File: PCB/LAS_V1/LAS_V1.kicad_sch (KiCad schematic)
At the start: 7 parts, among them J1 Conn_01x05_Socket, J2 Screw_Terminal_01x02, J4 Screw_Terminal_01x03, J5 Red_Conn_01x02_Pin, J6 Conn_01x18_Socket, J7 Conn_01x18_Socket, J9 Screw_Terminal_01x02

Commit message: -am
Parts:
- removed J2: Screw_Terminal_01x02, symbol Connector:Screw_Terminal_01x02
- added U2: ESP32-S2-MINI-1, Espressif:ESP32-S2-MINI-1, symbol ESP lib:ESP32-S2-MINI-1
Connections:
- net GND: now also U2.1 (GND), U2.2 (GND), U2.30 (GND), U2.42 (GND), U2.43 (GND), U2.46 (GND), U2.47 (GND), U2.48 (GND), U2.49 (GND), U2.50 (GND), U2.51 (GND), U2.52 (GND), U2.53 (GND), U2.54 (GND), U2.55 (GND), U2.56 (GND), U2.57 (GND), U2.58 (GND), U2.59 (GND), U2.60 (GND), U2.61 (GND), U2.62 (GND), U2.63 (GND), U2.64 (GND), U2.65 (GND)
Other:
- added sheet USB Interface (USB_interface.kicad_sch)
- sheet Power ports: added +3.3V; removed +12V
- sheet Relay Controls ports: added none; removed D1, D2, D3, D4, D5, D6, NO2, relay2
- moved on the sheet: J5

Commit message: installing JLB, PCB mostly done
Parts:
- removed U2: ESP32-S2-MINI-1, Espressif:ESP32-S2-MINI-1, symbol ESP lib:ESP32-S2-MINI-1
- added C4 (x3): 0.1uF, symbol Device:C_Small
- added C4 (x2): 10uF, symbol Device:C_Small
- added C4: 1uF, symbol Device:C_Small
- added R1: 10k, symbol Device:R_Small_US
- added SW1, SW2: SW_Push, symbol Switch:SW_Push
- added U1: ESP32-S3-WROOM-1, Espressif:ESP32-S3-WROOM-1, symbol ESP lib:ESP32-S3-WROOM-1
- added U2: AMS1117-3.3, Package_TO_SOT_SMD:SOT-223-3_TabPin2, symbol Regulator_Linear:AMS1117-3.3
- renumbered J9 to J1, J4 to J2, J5 to J3, J1 to J4, J7 to J5
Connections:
- net GND: now also C4.2, C4.2, C4.2, C4.2, C4.2, C4.2, SW1.1, SW2.1, U1.1 (GND), U1.40 (GND), U1.41 (GND), U2.1 (GND)
- net NC1: no longer J2.1 (Pin_1)
- net NO1: no longer names the net of J2.2 (Pin_2)
- new net +3.3V: C4.1, C4.1, C4.1, R1.1, U1.2 (3V3), U2.2 (VO)
- new net BOOT_SEL: C4.1, SW1.2, U1.27 (GPIO0/BOOT)
- new net CHIP_PU: C4.1, C4.1, R1.2, SW2.2, U1.3 (EN)
- new net DIN_3.3: U1.5 (GPIO5/TOUCH5/ADC1_CH4)
- new net GPIO1: U1.38 (GPIO2/TOUCH2/ADC1_CH1)
- new net GPIO2: U1.15 (GPIO3/TOUCH3/ADC1_CH2)
- new net GPIO3: U1.4 (GPIO4/TOUCH4/ADC1_CH3)
- new net GPIO6: U1.6 (GPIO6/TOUCH6/ADC1_CH5)
- new net RX1: U1.7 (GPIO7/TOUCH7/ADC1_CH6)
- new net RXD0: U1.36 (U0RXD/GPIO44/CLK_OUT2)
- new net TXD0: U1.37 (U0TXD/GPIO43/CLK_OUT1)
- new net VCC_5V: U2.3 (VI)
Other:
- removed sheet Power
- added sheet AC Monitor (AC_Monitor_sch.kicad_sch)
- added sheet Level Shifter (Level_shifter.kicad_sch)
- sheet LEDs ports: added +5V, DIN; removed none
- sheet Relay Controls ports: added +5V, COM, relay_act; removed relay1, relay_input1, relay_input2
- sheet USB Interface ports: added +3.3V, BOOT_SEL, CHIP_PU, RXD0, TXD0, VBus, VCC_5V; removed none
- moved on the sheet: J4, J5, J6

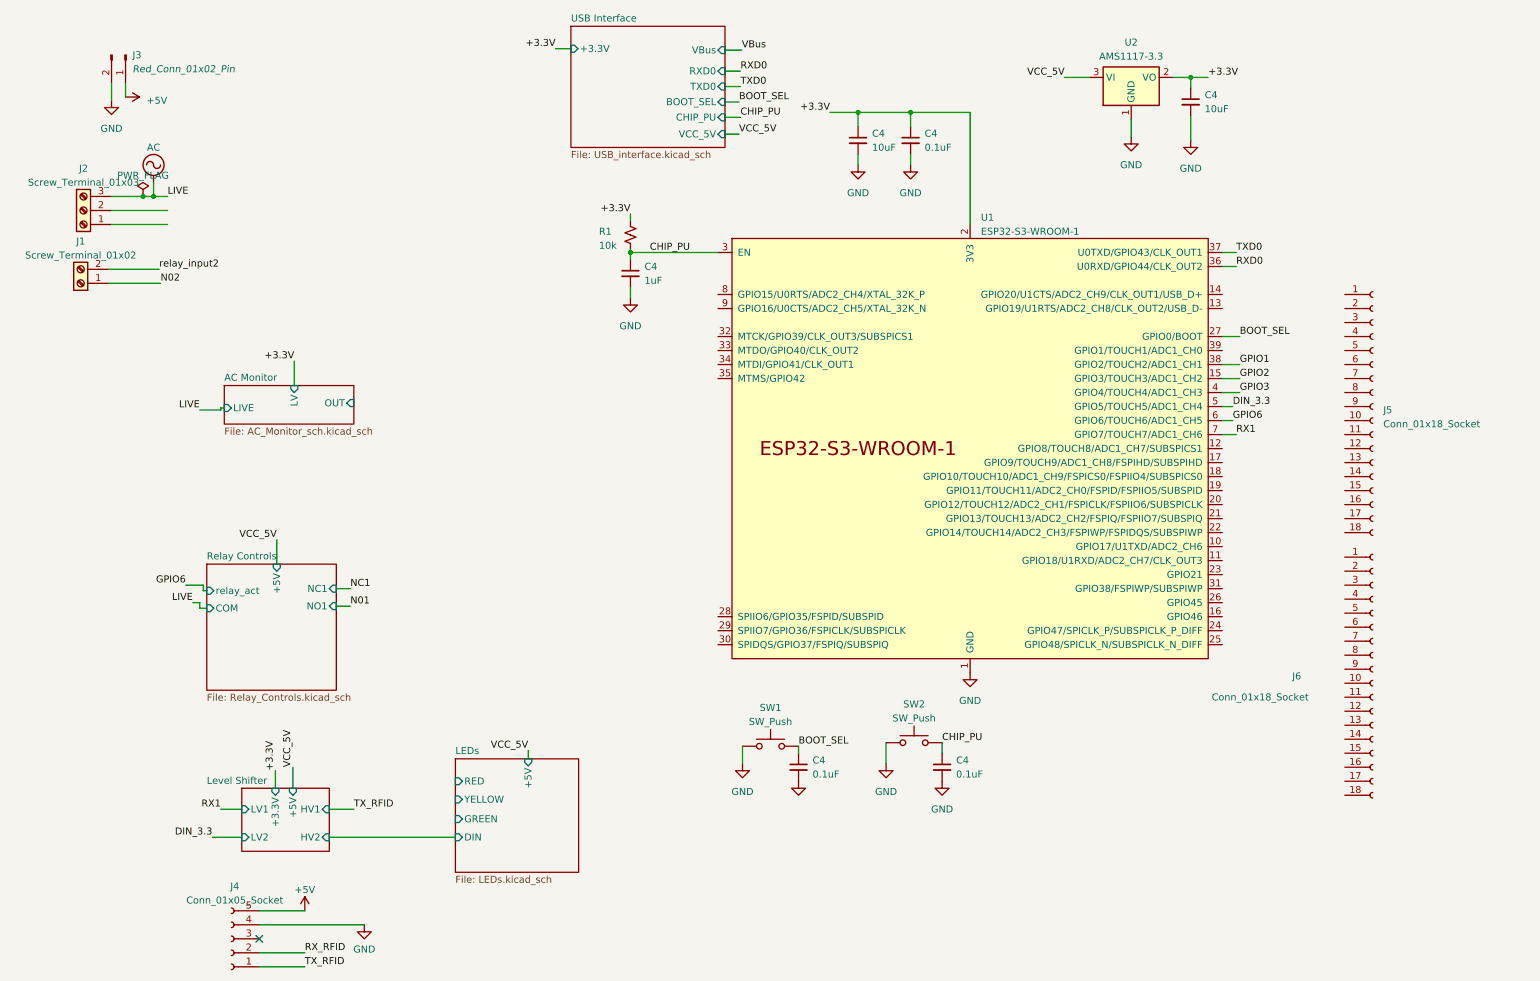
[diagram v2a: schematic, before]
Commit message: added JLBPCB part Numbers
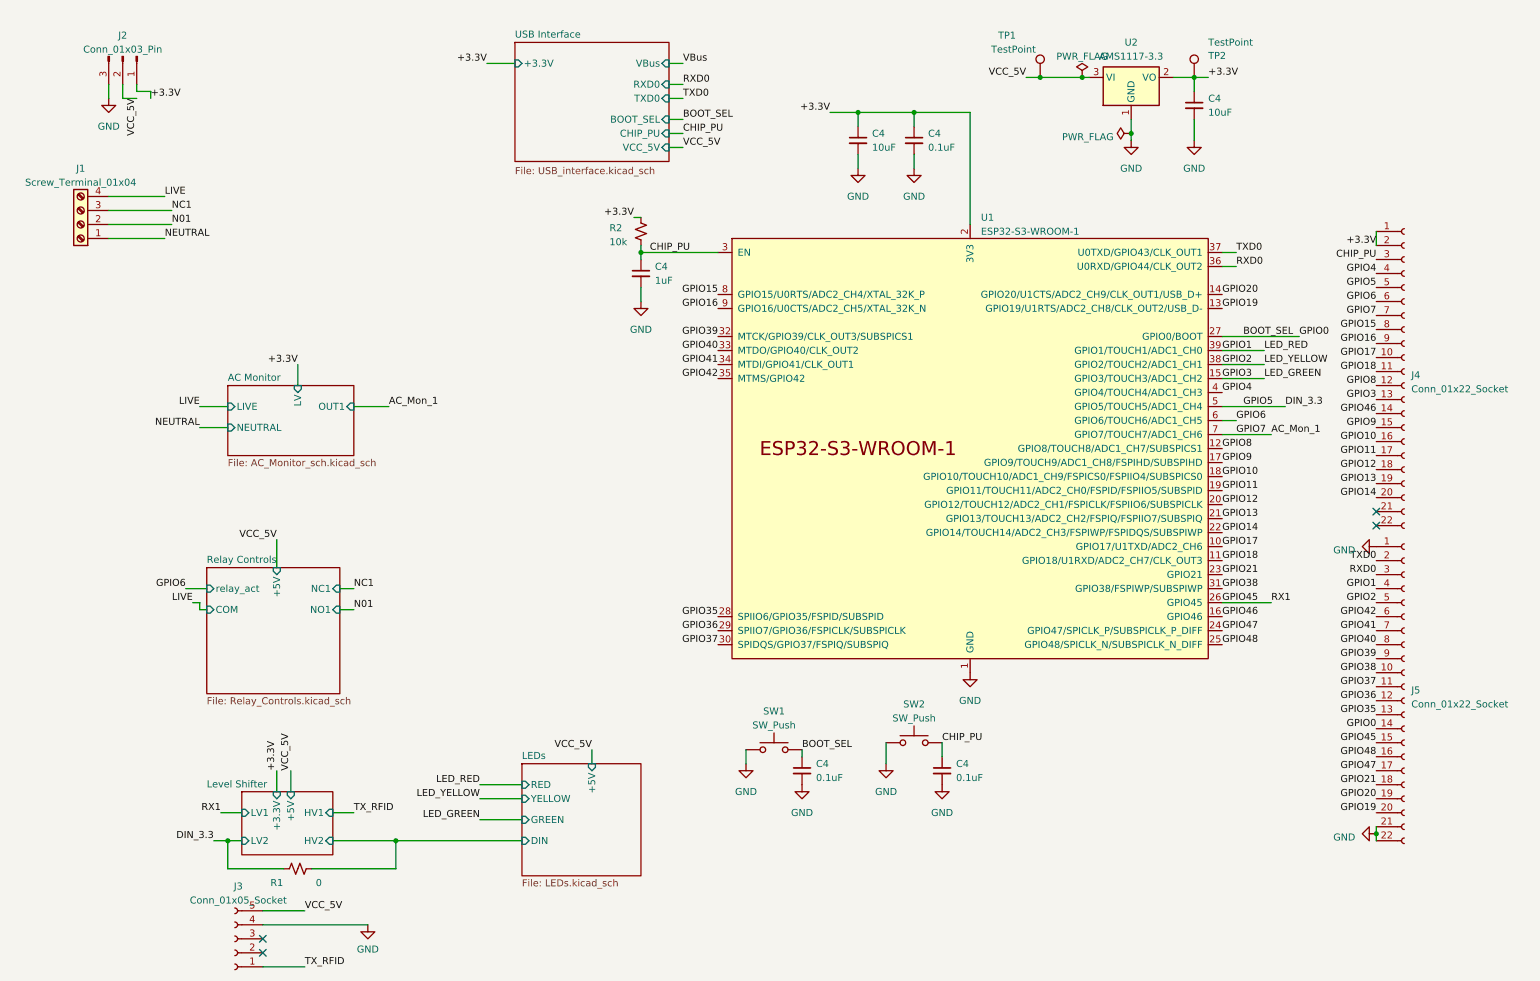
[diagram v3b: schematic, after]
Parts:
- removed J1: Screw_Terminal_01x02, symbol Connector:Screw_Terminal_01x02
- removed J2: Screw_Terminal_01x03, symbol Connector:Screw_Terminal_01x03
- removed J3: Red_Conn_01x02_Pin, symbol Connector:Conn_01x02_Pin
- removed J5, J6: Conn_01x18_Socket, symbol Connector:Conn_01x18_Socket
- added J1: Screw_Terminal_01x04, TerminalBlock_Phoenix:TerminalBlock_Phoenix_MKDS-1,5-4-5.08_1x04_P5.08mm_Horizontal, symbol Connector:Screw_Terminal_01x04
- added J2: Conn_01x03_Pin, Connector_PinHeader_1.27mm:PinHeader_1x03_P1.27mm_Vertical, symbol Connector:Conn_01x03_Pin
- added J4, J5: Conn_01x22_Socket, Connector_PinHeader_1.27mm:PinHeader_1x22_P1.27mm_Vertical, symbol Connector:Conn_01x22_Socket
- added R1: 0, Resistor_SMD:R_0603_1608Metric, symbol Device:R_Small_US
- added TP1, TP2: TestPoint, TestPoint:TestPoint_Pad_D1.5mm, symbol Connector:TestPoint
- C4: footprint (none) -> Capacitor_SMD:C_0603_1608Metric; LCSC (none) -> C14663
- C4: footprint (none) -> Capacitor_SMD:C_0603_1608Metric; LCSC (none) -> C19702
- C4: footprint (none) -> Capacitor_SMD:C_0603_1608Metric; LCSC (none) -> C15849
- J3: renamed from J4; footprint (none) -> Connector_PinHeader_1.27mm:PinHeader_1x05_P1.27mm_Vertical
- R2: renamed from R1; footprint (none) -> Resistor_SMD:R_1206_3216Metric; LCSC (none) -> C17902
- SW1, SW2: footprint (none) -> Connector_PinHeader_1.27mm:PinHeader_1x02_P1.27mm_Vertical; LCSC (none) -> C2844397
- U1: LCSC (none) -> C2913200
- U2: LCSC (none) -> C6186
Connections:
- net +5V is gone; now on net VCC_5V: J3.5 (Pin_5)
- net +3.3V: now also J2.1 (Pin_1), J4.1 (Pin_1), J4.2 (Pin_2), TP2.1
- net BOOT_SEL: now also J5.14 (Pin_14)
- net CHIP_PU: now also J4.3 (Pin_3)
- net DIN_3.3: now also J4.5 (Pin_5), R1.2
- net GND: now also J2.3 (Pin_3), J5.1 (Pin_1), J5.21 (Pin_21), J5.22 (Pin_22)
- net GPIO1: now also U1.39 (GPIO1/TOUCH1/ADC1_CH0), J5.4 (Pin_4); no longer U1.38 (GPIO2/TOUCH2/ADC1_CH1)
- net GPIO2: now also U1.38 (GPIO2/TOUCH2/ADC1_CH1), J5.5 (Pin_5); no longer U1.15 (GPIO3/TOUCH3/ADC1_CH2)
- net GPIO3: now also U1.15 (GPIO3/TOUCH3/ADC1_CH2), J4.13 (Pin_13); no longer U1.4 (GPIO4/TOUCH4/ADC1_CH3)
- net GPIO6: now also J4.6 (Pin_6)
- net LEDs/DIN: now also R1.1
- net N01: now also J1.2 (Pin_2)
- net NC1: now also J1.3 (Pin_3)
- net RXD0: now also J5.3 (Pin_3)
- net TXD0: now also J5.2 (Pin_2)
- net VCC_5V: now also J2.2 (Pin_2), TP1.1
- net GPIO17: now reaches U1.10 (GPIO17/U1TXD/ADC2_CH6)
- net GPIO17: now also J4.10 (Pin_10)
- net GPIO18: now reaches U1.11 (GPIO18/U1RXD/ADC2_CH7/CLK_OUT3)
- net GPIO18: now also J4.11 (Pin_11)
- net GPIO8: now reaches U1.12 (GPIO8/TOUCH8/ADC1_CH7/SUBSPICS1)
- net GPIO8: now also J4.12 (Pin_12)
- net GPIO19: now reaches U1.13 (GPIO19/U1RTS/ADC2_CH8/CLK_OUT2/USB_D-)
- net GPIO19: now also J5.20 (Pin_20)
- net GPIO20: now reaches U1.14 (GPIO20/U1CTS/ADC2_CH9/CLK_OUT1/USB_D+)
- net GPIO20: now also J5.19 (Pin_19)
- net GPIO46: now reaches U1.16 (GPIO46)
- net GPIO46: now also J4.14 (Pin_14)
- net GPIO9: now reaches U1.17 (GPIO9/TOUCH9/ADC1_CH8/FSPIHD/SUBSPIHD)
- net GPIO9: now also J4.15 (Pin_15)
- net GPIO10: now reaches U1.18 (GPIO10/TOUCH10/ADC1_CH9/FSPICS0/FSPIIO4/SUBSPICS0)
- net GPIO10: now also J4.16 (Pin_16)
- net GPIO11: now reaches U1.19 (GPIO11/TOUCH11/ADC2_CH0/FSPID/FSPIIO5/SUBSPID)
- net GPIO11: now also J4.17 (Pin_17)
- net GPIO12: now reaches U1.20 (GPIO12/TOUCH12/ADC2_CH1/FSPICLK/FSPIIO6/SUBSPICLK)
- net GPIO12: now also J4.18 (Pin_18)
- net GPIO13: now reaches U1.21 (GPIO13/TOUCH13/ADC2_CH2/FSPIQ/FSPIIO7/SUBSPIQ)
- net GPIO13: now also J4.19 (Pin_19)
- net GPIO14: now reaches U1.22 (GPIO14/TOUCH14/ADC2_CH3/FSPIWP/FSPIDQS/SUBSPIWP)
- net GPIO14: now also J4.20 (Pin_20)
- net GPIO21: now reaches U1.23 (GPIO21)
- net GPIO21: now also J5.18 (Pin_18)
- net GPIO47: now reaches U1.24 (GPIO47/SPICLK_P/SUBSPICLK_P_DIFF)
- net GPIO47: now also J5.17 (Pin_17)
- net GPIO48: now reaches U1.25 (GPIO48/SPICLK_N/SUBSPICLK_N_DIFF)
- net GPIO48: now also J5.16 (Pin_16)
- net GPIO45: now reaches U1.26 (GPIO45)
- net GPIO45: now also J5.15 (Pin_15)
- net GPIO35: now reaches U1.28 (SPIIO6/GPIO35/FSPID/SUBSPID)
- net GPIO35: now also J5.13 (Pin_13)
- net GPIO36: now reaches U1.29 (SPIIO7/GPIO36/FSPICLK/SUBSPICLK)
- net GPIO36: now also J5.12 (Pin_12)
- net GPIO37: now reaches U1.30 (SPIDQS/GPIO37/FSPIQ/SUBSPIQ)
- net GPIO37: now also J5.11 (Pin_11)
- net GPIO38: now reaches U1.31 (GPIO38/FSPIWP/SUBSPIWP)
- net GPIO38: now also J5.10 (Pin_10)
- net GPIO39: now reaches U1.32 (MTCK/GPIO39/CLK_OUT3/SUBSPICS1)
- net GPIO39: now also J5.9 (Pin_9)
- net GPIO40: now reaches U1.33 (MTDO/GPIO40/CLK_OUT2)
- net GPIO40: now also J5.8 (Pin_8)
- net GPIO41: now reaches U1.34 (MTDI/GPIO41/CLK_OUT1)
- net GPIO41: now also J5.7 (Pin_7)
- net GPIO42: now reaches U1.35 (MTMS/GPIO42)
- net GPIO42: now also J5.6 (Pin_6)
- net GPIO15: now reaches U1.8 (GPIO15/U0RTS/ADC2_CH4/XTAL_32K_P)
- net GPIO15: now also J4.8 (Pin_8)
- net GPIO16: now reaches U1.9 (GPIO16/U0CTS/ADC2_CH5/XTAL_32K_N)
- net GPIO16: now also J4.9 (Pin_9)
- net RX1 renamed AC_Mon_1
- net AC_Mon_1: now also J4.7 (Pin_7)
- net RX_RFID: no longer names the net of J3.2 (Pin_2)
- new net GPIO4: J4.4 (Pin_4), U1.4 (GPIO4/TOUCH4/ADC1_CH3)
- new net LIVE: J1.4 (Pin_4)
- new net NEUTRAL: J1.1 (Pin_1)
- no-connect marks 1 -> 4
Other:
- sheet AC Monitor ports: added NEUTRAL, OUT1; removed OUT
- moved on the sheet: C4, J3, R2, SW1
